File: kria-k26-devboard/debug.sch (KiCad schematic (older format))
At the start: 70 parts, among them J8 USB4105-GF-A, J9 0878311420, Q10 DTC014TEBTL, Q17 DTC014TEBTL, Q9 DTC014TEBTL, U28 WE-TVS-82400152, U29 MIC5211-3.3YM6-TR, U30 FT4232HPQ, U31 93LC56CT-IMC, U32 74AVC4T245RSVRG4, U33 74AVC4T245RSVRG4, U34 SN74AVC2T245RSWR, U35 SN74AVC2T245RSWR, U36 NC7WZ07P6X, U54 TPD4E05U06QDQARQ1, Y5 ABM8G-12.000MHZ-18-D2Y-T

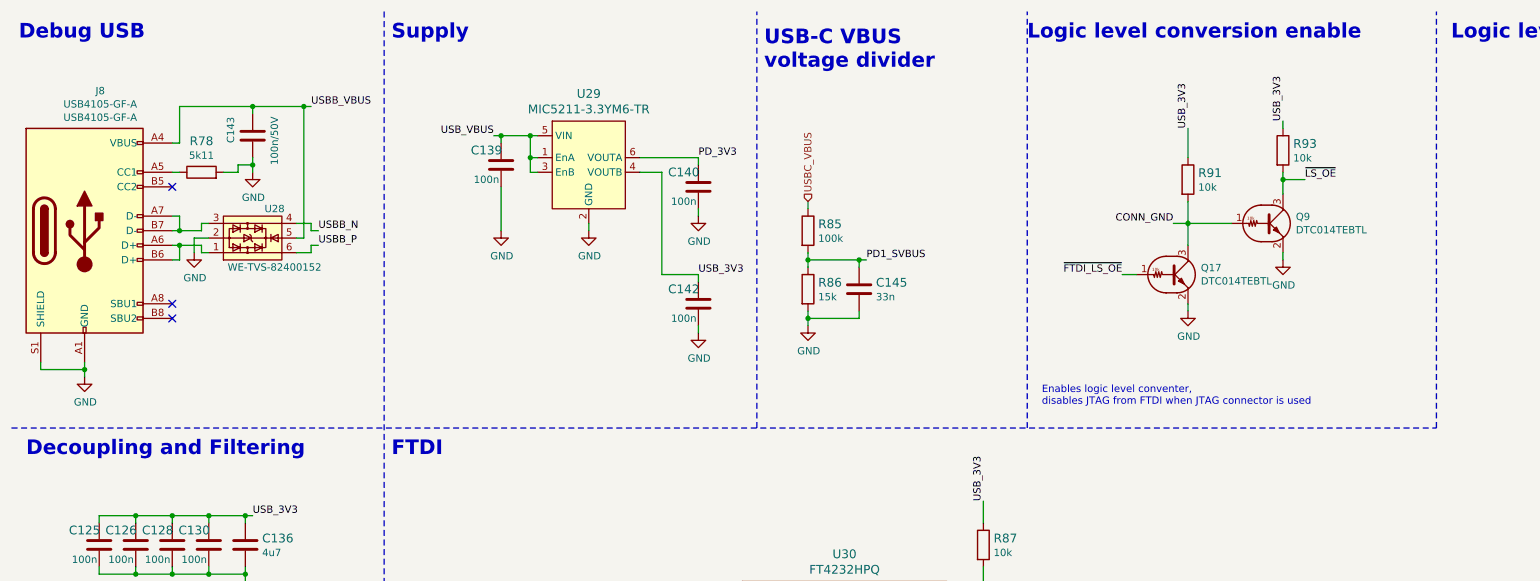
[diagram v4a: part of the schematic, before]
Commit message: Optimization of power planes, fixed missing capacitors on USB 3.0, unify shields, polishing of layout
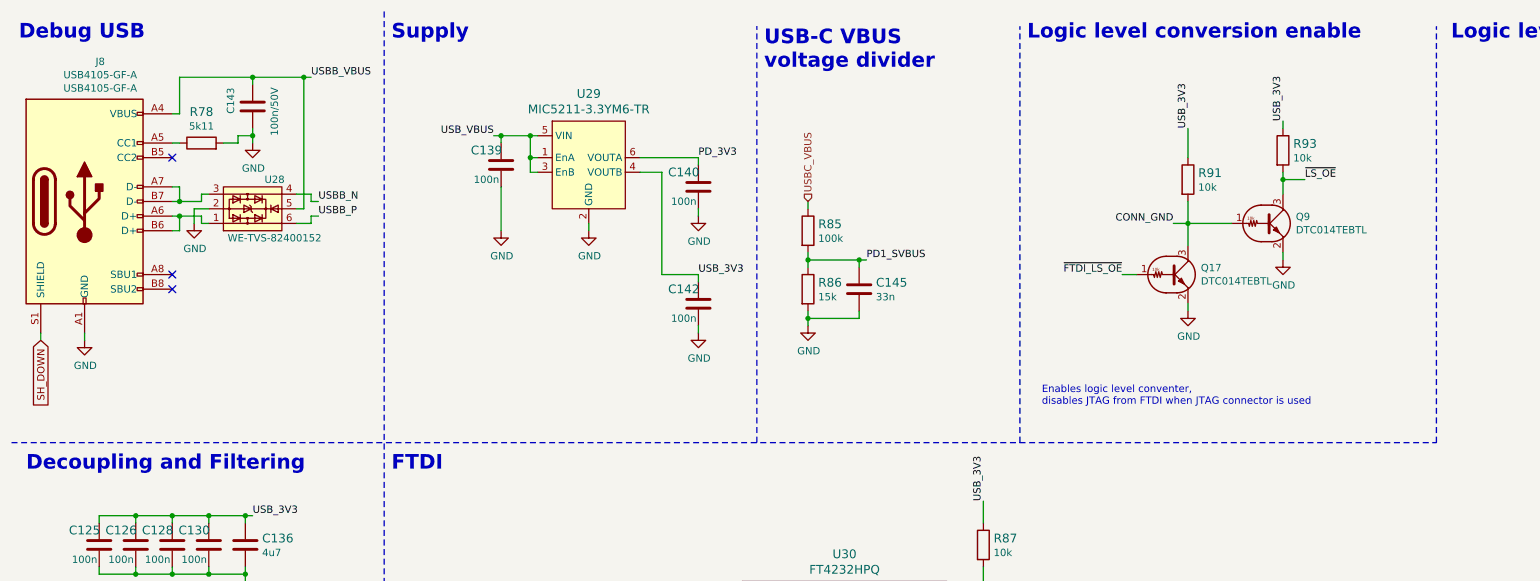
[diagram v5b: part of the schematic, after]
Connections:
- net GND: no longer J8.S1 (SHIELD)
- new net SH_DOWN: J8.S1 (SHIELD)
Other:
- moved on the sheet: C143, J8, R78, U28

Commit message: Fixed missing USB - M2 connection, finishing touches of PCB
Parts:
- added TP21, TP22, TP23, TP24, TP25, TP26, TP27, TP28, TP29, TP30: TP_SMD_0_75MM, antmicro-footprints:Testpoint_smd_0_75mm, symbol antmicroTestPoints:TP_SMD_0_75MM
- renumbered C125 to C146, C127 to C147, C126 to C148, C129 to C149, C128 to C150, C131 to C151, C130 to C152, C133 to C153, C134 to C154, C135 to C155, C136 to C156, C137 to C157, C138 to C158, C143 to C159, C139 to C160, C141 to C161, C144 to C162, C140 to C163, C142 to C164, C146 to C165, C145 to C166, C147 to C167, C148 to C168, C149 to C169, C150 to C170, C151 to C171, C152 to C172, C153 to C173, C154 to C174, C155 to C175, C156 to C176, D25 to D7, Q17 to Q10, Q9 to Q11, Q10 to Q12, R80 to R100, R78 to R101, R81 to R102, R82 to R103, R83 to R104, R84 to R105, R85 to R106, R86 to R107, R87 to R108, R88 to R109, R89 to R110, R90 to R111, R92 to R112, R91 to R113, R93 to R114, R95 to R115, R96 to R116, R79 to R99, U28 to U37, U29 to U38, U30 to U39, U31 to U40, U54 to U41, U32 to U42, U33 to U43, U34 to U44, U35 to U45, U36 to U46, Y5 to Y7
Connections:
- net CONN_GND: now also TP28.1
- net PD1_SVBUS: now also TP26.1
- net USB_1V2: now also TP21.1
- net USB_3V3: now also TP24.1
- net VCC_PD: now also TP22.1
- net VCC_USB: now also TP25.1
- net VREGIN: now also TP23.1
- net ~EEPROM_WC: now also TP30.1
- net ~FTDI_LS_OE: now also TP27.1
- net ~LS_OE: now also TP29.1
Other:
- moved on the sheet: C166
